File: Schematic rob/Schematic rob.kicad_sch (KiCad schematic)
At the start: 2 parts, among them Q1 C2M0080120D, Q2 C2M0080120D

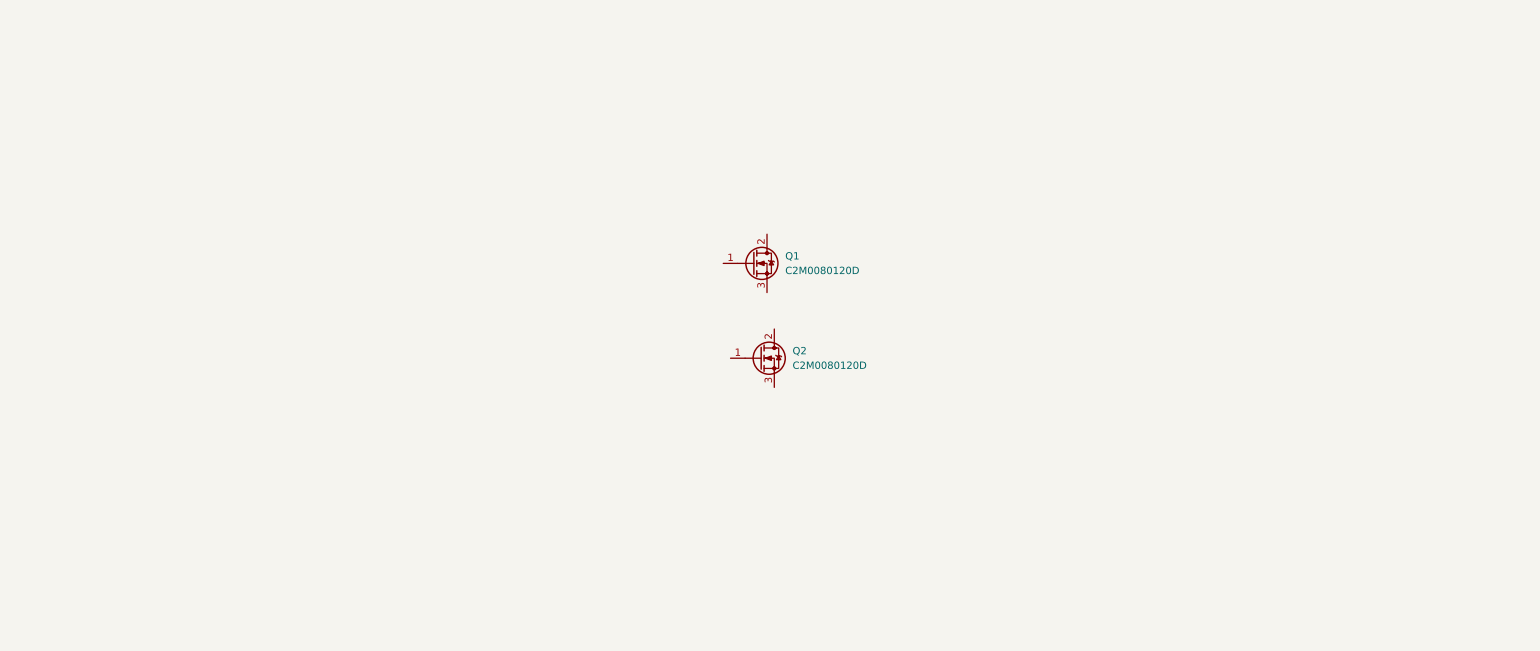
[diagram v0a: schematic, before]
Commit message: Updated schematic and added datasheets
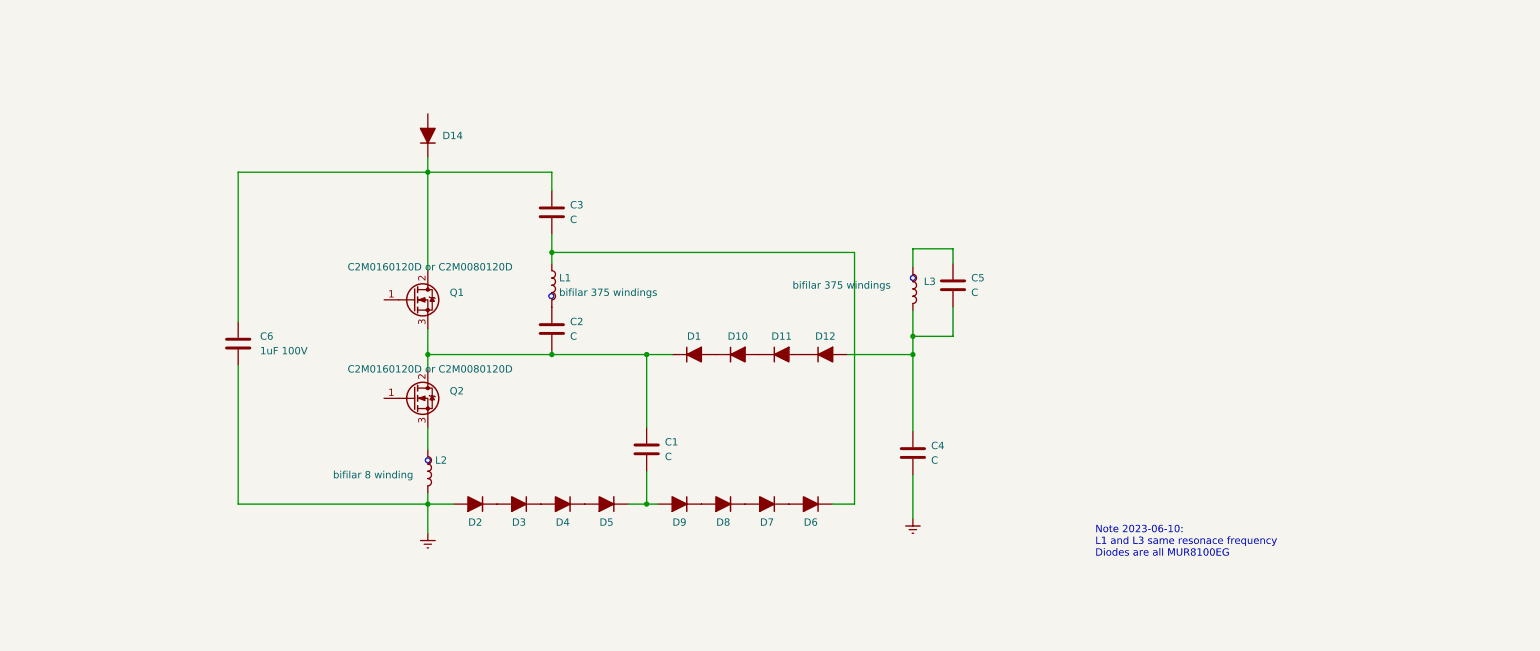
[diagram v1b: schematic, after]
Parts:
- added C1, C2, C3, C4, C5: C, symbol Device:C
- added C6: 1uF 100V, symbol Device:C
- added D1, D10, D11, D12, D14, D2, D3, D4, D5, D6, D7, D8, D9: D_Filled, symbol Device:D_Filled
- added L1, L3: bifilar 375 windings, symbol Device:L
- added L2: bifilar 8 winding, symbol Device:L
- Q1: value C2M0080120D -> C2M0160120D or C2M0080120D; Note (none) -> Ordered from Amamzon. as FGA25N120 (https://www.amazon.co.j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
- Q2: value C2M0080120D -> C2M0160120D or C2M0080120D
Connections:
- net at Q1.2 (D): now also C3.1, C6.1, D14.1 (K)
- net at Q1.3 (S): now also Q2.2 (D), C1.1, C2.2, D1.1 (K)
- net at Q2.3 (S): now also L2.1
- new net: C5.1, L3.1
- new net: C4.1, C5.2, D12.2 (A), L3.2
- new net: C2.1, L1.2
- new net: D6.2 (A), D7.1 (K)
- new net: D7.2 (A), D8.1 (K)
- new net: D11.2 (A), D12.1 (K)
- new net: C1.2, D5.1 (K), D9.2 (A)
- new net: D8.2 (A), D9.1 (K)
- new net: C3.2, D6.1 (K), L1.1
- new net: D1.2 (A), D10.1 (K)
- new net: D10.2 (A), D11.1 (K)
- new net: D4.1 (K), D5.2 (A)
- new net: D2.1 (K), D3.2 (A)
- new net: D3.1 (K), D4.2 (A)
- new net Earth: C4.2, C6.2, D2.2 (A), L2.2
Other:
- note added: "Note 2023-06-10: L1 and L3 same resonace frequency Diodes are all MUR8100EG"
- company: (none) -> YR-Design
- title: (none) -> IVO Spiker
- moved on the sheet: Q1, Q2

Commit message: updated schematic
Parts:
- added U1: Si5351A-B-GT, Package_SO:MSOP-10_3x3mm_P0.5mm, symbol Oscillator:Si5351A-B-GT
- added U2: ESP32-WROOM-32, RF_Module:ESP32-WROOM-32, symbol RF_Module:ESP32-WROOM-32
- L1, L3: value bifilar 375 windings -> bifiar 272 windings
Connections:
- new net: U2.1 (GND), U2.15 (GND), U2.38 (GND), U2.39 (GND)
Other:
- moved on the sheet: C1, C2, C3, C4, C5, C6, D1, D10, D11, D12, D14, D2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

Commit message: Updated schematic and extra docs
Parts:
- added R1, R2: 3.3, symbol Device:R
- added R3, R4: 50, symbol Device:R
- added U3: IR2213, Package_DIP:DIP-14_W7.62mm, symbol Driver_FET:IR2213
- L1: value bifiar 272 windings -> bifia19 windings
- L3: value bifiar 272 windings -> biflar 22 windings
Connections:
- net Earth: now also R4.1, U3.13 (VSS), U3.2 (COM)
- net at U2.20 (SCK/CLK): now also U1.4 (SCL)
- net at U1.1 (VDD): now also U3.9 (VDD)
- net at U1.10 (CLK0): now also R3.1
- net at Q1.1 (G): now also R1.2
- net at Q2.1 (G): now also R2.2
- new net: R1.1, U3.7 (HO)
- new net: R2.1, U3.1 (LO)
- new net: R3.2, R4.2, U3.10 (HIN), U3.12 (LIN)
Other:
- note added: "tank circuit IVO got 5A 100V for input 65 watt(66V 1A)"
- moved on the sheet: C6, U1, U2

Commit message: updated board data
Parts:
- removed R3: 50, symbol Device:R
- removed U2: ESP32-WROOM-32, RF_Module:ESP32-WROOM-32, symbol RF_Module:ESP32-WROOM-32
- added SW1: RotaryEncoder_Switch, symbol Library:RotaryEncoder_Switch
- added U1: SSD1306, Package_TO_SOT_SMD:SOT-23-5, symbol Library:24AA02-OT
- added U2: L7805, symbol Regulator_Linear:L7805
- added U5: ESP32_NODEMCU, MODULE_ESP32_NODEMCU, symbol Library:ESP32_NODEMCU
- C1, C2, C3, C4, C5, C6: symbol Device:C -> Library:C
- D1, D10, D11, D12, D14, D2, D3, D4, D5, D6, D7, D8, D9: symbol Device:D_Filled -> Library:D_Filled
- L1, L2, L3: symbol Device:L -> Library:L
- Q1, Q2: symbol Transistor_FET:C2M0080120D -> Library:C2M0080120D
- R1, R2, R4: symbol Device:R -> Library:R
- U1: symbol Oscillator:Si5351A-B-GT -> Library:Si5351A-B-GT
- U3: symbol Driver_FET:IR2213 -> Library:IR2213
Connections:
- net Earth: now also SW1.C, SW1.S1, U1.1 (GND), U2.2 (GND), U5.J5_6 (GND_J5_6)
- net at U1.4 (SCL): now also U1.3 (SCL)
- net at R4.2, U3.10 (HIN), U3.12 (LIN): now also U1.10 (CLK0)
- net at U1.1 (VDD), U3.9 (VDD): now also U5.J5_19 (3V3)
- net at U1.5 (SDA): now also SW1.B, U1.4 (SDA), U5.J4_3 (G22), U5.J4_6 (G21), U5.J5_11 (G25)
- net +15V: now reaches D14.2 (A)
- net +15V: now also U2.1 (IN)
- new net: SW1.A, U5.J4_2 (G23)
- new net: U2.3 (OUT), U5.J5_1 (5V)
- new net: SW1.S2, U5.J5_10 (G26)
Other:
- note added: "tank circuit IVO got 4.3A 100V for input 65 watt(66V 1A)"
- note removed: "tank circuit IVO got 5A 100V for input 65 watt(66V 1A)"
- moved on the sheet: C1, C2, C3, C4, C5, C6, D1, D10, D11, D12, D14, D2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

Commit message: Updated schematic
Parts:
- removed C1, C4: C, symbol Library:C
- removed D1, D10, D11, D12, D2, D3, D4, D5, D6, D7, D8, D9: D_Filled, symbol Library:D_Filled
- added D13, D15: 4007, symbol Device:D
- L2: value bifilar 8 winding -> Special winded bifilar
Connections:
- net Earth: now also C5.2, L3.2
- net at R1.1, U3.7 (HO): now also D13.1 (K)
- net at Q1.1 (G), R1.2: now also D13.2 (A)
- net at R2.1, U3.1 (LO): now also D15.1 (K)
- net at Q2.1 (G), R2.2: now also D15.2 (A)
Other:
- note added: "bifil but special connected see https://t.ly/yhPj"
- moved on the sheet: C5, C6, L3

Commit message: Updated schematic
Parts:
- L1: value bifia19 windings -> bifilar 19 windings
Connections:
- net Earth: no longer U3.13 (VSS)
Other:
- note added: "bifilar but special connected see https://t.ly/yhPj"
- note removed: "bifil but special connected see https://t.ly/yhPj"
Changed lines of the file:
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@@
   (junction (at 165.1 76.2) (diameter 0) (color 0 0 0 0)
   )
-  (junction (at 121.285 81.915) (diameter 0) (color 0 0 0 0)
-  )
   (junction (at 144.145 76.2) (diameter 0) (color 0 0 0 0)
   )
-  (junction (at 113.03 81.915) (diameter 0) (color 0 0 0 0)
-  )
   (junction (at 88.265 48.895) (diameter 0) (color 0 0 0 0)
   )
+  (junction (at 113.03 83.82) (diameter 0) (color 0 0 0 0)
+  )
   (junction (at 75.565 117.475) (diameter 0) (color 0 0 0 0)
   )
@@
     (stroke (width 0) (type default))
   )
-  (wire (pts (xy 69.85 32.385) (xy 125.095 32.385))
-    (stroke (width 0) (type default))
-  )
-  (wire (pts (xy 123.825 81.915) (xy 121.285 81.915))
-    (stroke (width 0) (type default))
-  )
   (wire (pts (xy 186.944 75.565) (xy 186.944 76.2))
     (stroke (width 0) (type default))
@@
     (stroke (width 0) (type default))
   )
+  (wire (pts (xy 123.825 81.28) (xy 123.825 83.82))
+    (stroke (width 0) (type default))
+  )
   (wire (pts (xy 165.1 76.2) (xy 186.944 76.2))
     (stroke (width 0) (type default))
@@
     (stroke (width 0) (type default))
   )
+  (wire (pts (xy 113.03 83.82) (xy 123.825 83.82))
+    (stroke (width 0) (type default))
+  )
   (wire (pts (xy 144.145 76.2) (xy 147.955 76.2))
     (stroke (width 0) (type default))
@@
     (stroke (width 0) (type default))
   )
-  (wire (pts (xy 121.285 81.28) (xy 121.285 81.915))
-    (stroke (width 0) (type default))
-  )
-  (wire (pts (xy 121.285 81.915) (xy 113.03 81.915))
-    (stroke (width 0) (type default))
-  )
   (wire (pts (xy 165.1 44.45) (xy 165.1 61.595))
     (stroke (width 0) (type default))
@@
     (stroke (width 0) (type default))
   )
-  (wire (pts (xy 69.85 31.75) (xy 69.85 32.385))
-    (stroke (width 0) (type default))
-  )
   (wire (pts (xy 150.495 102.235) (xy 165.354 102.235))
     (stroke (width 0) (type default))
   )
-  (wire (pts (xy 88.265 48.26) (xy 88.265 48.895))
+  (wire (pts (xy 113.03 81.915) (xy 113.03 83.82))
     (stroke (width 0) (type default))
   )
@@
     (stroke (width 0) (type default))
   )
-  (wire (pts (xy 72.39 48.26) (xy 72.39 67.945))
+  (wire (pts (xy 72.39 48.895) (xy 72.39 67.945))
     (stroke (width 0) (type default))
   )
@@
     (stroke (width 0) (type default))
   )
-  (wire (pts (xy 68.58 31.75) (xy 69.85 31.75))
+  (wire (pts (xy 68.58 32.385) (xy 125.095 32.385))
     (stroke (width 0) (type default))
   )
@@
     (stroke (width 0) (type default))
   )
-  (wire (pts (xy 123.825 81.28) (xy 123.825 81.915))
-    (stroke (width 0) (type default))
-  )
   (wire (pts (xy 68.58 100.965) (xy 71.755 100.965))
     (stroke (width 0) (type default))
@@
     (stroke (width 0) (type default))
   )
-  (wire (pts (xy 72.39 48.26) (xy 88.265 48.26))
-    (stroke (width 0) (type default))
-  )
-  (wire (pts (xy 68.58 65.405) (xy 68.58 31.75))
+  (wire (pts (xy 72.39 48.895) (xy 88.265 48.895))
+    (stroke (width 0) (type default))
+  )
+  (wire (pts (xy 68.58 65.405) (xy 68.58 32.385))
     (stroke (width 0) (type default))
   )
@@
   )
   (wire (pts (xy 165.354 107.315) (xy 165.354 102.235))
+    (stroke (width 0) (type default))
+  )
+  (wire (pts (xy 113.03 83.82) (xy 113.03 85.09))
     (stroke (width 0) (type default))
   )
@@
     (effects (font (size 1.27 1.27)) (justify left bottom))
   )
-  (text "bifil but special \nconnected see  https://t.ly/yhPj " (exclude_from_sim no)
+  (text "bifilar but special \nconnected see  https://t.ly/yhPj " (exclude_from_sim no)
     (at 167.005 92.71 0)
     (effects (font (size 1.27 1.27)) (justify left bottom))
@@
       (effects (font (size 1.27 1.27)) (justify left))
     )
-    (property "Value" "biflar 22 windings" (at 194.818 55.372 0)
+    (property "Value" "biflar 22 windings" (at 196.215 69.85 90)
       (effects (font (size 1.27 1.27)) (justify left))
     )
@@
     )
   )
-  (symbol (lib_id "power:Earth") (at 113.03 81.915 0) (unit 1)
-    (in_bom yes) (on_board yes) (dnp no) (fields_autoplaced)
-    (property "Reference" "#PWR03" (at 113.03 88.265 0)
-      (effects (font (size 1.27 1.27)) hide)
-    )
-    (property "Value" "Earth" (at 113.03 85.725 0)
-      (effects (font (size 1.27 1.27)) hide)
-    )
-    (property "Footprint" "" (at 113.03 81.915 0)
-      (effects (font (size 1.27 1.27)) hide)
-    )
-    (property "Datasheet" "~" (at 113.03 81.915 0)
-      (effects (font (size 1.27 1.27)) hide)
-    )
-    (property "Description" "" (at 113.03 81.915 0)
+  (symbol (lib_id "power:Earth") (at 113.03 85.09 0) (unit 1)
+    (in_bom yes) (on_board yes) (dnp no) (fields_autoplaced)
+    (property "Reference" "#PWR03" (at 113.03 91.44 0)
+      (effects (font (size 1.27 1.27)) hide)
+    )
+    (property "Value" "Earth" (at 113.03 88.9 0)
+      (effects (font (size 1.27 1.27)) hide)
+    )
+    (property "Footprint" "" (at 113.03 85.09 0)
+      (effects (font (size 1.27 1.27)) hide)
+    )
+    (property "Datasheet" "~" (at 113.03 85.09 0)
+      (effects (font (size 1.27 1.27)) hide)
+    )
+    (property "Description" "" (at 113.03 85.09 0)
       (effects (font (size 1.27 1.27)) hide)
     )
@@
       (effects (font (size 1.27 1.27)) (justify left))
     )
-    (property "Value" "bifia19 windings" (at 177.292 64.008 0)
-      (effects (font (size 1.27 1.27)) (justify left))
-    )
+    (property "Value" "bifilar 19 windings" (at 185.42 69.85 90)
+      (effects (font (size 1.27 1.27)) (justify left))
+    )

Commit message: Init
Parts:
- D14: value D_Filled -> MUR8100EG
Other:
- note added: "Note 2023-06-10: L1 and L3 same resonace frequency"
- note removed: "Note 2023-06-10: L1 and L3 same resonace frequency Diodes are all MUR8100EG"
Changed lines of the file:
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@@
     (fill (type color) (color 134 0 46 1))
   )
-  (text "\nNote 2023-06-10:\nL1 and L3 same resonace frequency\nDiodes are all MUR8100EG\n\n" (exclude_from_sim no)
+  (text "\nNote 2023-06-10:\nL1 and L3 same resonace frequency\n\n\n" (exclude_from_sim no)
     (at 203.2 131.445 0)
     (effects (font (size 1.27 1.27)) (justify left bottom))
@@
   )
   (symbol (lib_id "Library:D_Filled") (at 165.1 38.1 90) (unit 1)
-    (in_bom yes) (on_board yes) (dnp no) (fields_autoplaced)
+    (in_bom yes) (on_board yes) (dnp no)
     (property "Reference" "D14" (at 167.64 38.1 90)
       (effects (font (size 1.27 1.27)) (justify right))
     )
-    (property "Value" "D_Filled" (at 167.64 39.37 90)
-      (effects (font (size 1.27 1.27)) (justify right) hide)
+    (property "Value" "MUR8100EG" (at 166.37 40.64 90)
+      (effects (font (size 1.27 1.27)) (justify right))
     )
     (property "Footprint" "" (at 165.1 38.1 0)
